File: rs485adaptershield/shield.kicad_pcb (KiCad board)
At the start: 2 copper layers, 68.6 x 53.3 mm, 8 parts, among them U2 Analog_1, U3 Analog_2, U6 Digital_1, U7 Digital_2

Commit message: schematic mostly finished w/o footprints
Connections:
- U2 pad 4: unconnected-(U2-Pad4) -> +3.3V
- U2 pad 5: unconnected-(U2-Pad5) -> +5V
- U2 pad 6: unconnected-(U2-Pad6) -> GND
- U2 pad 7: unconnected-(U2-Pad7) -> GND
- U2 pad 8: unconnected-(U2-Pad8) -> VBATT
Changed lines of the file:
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@@
 			)
 		)
-		(sheetfile "ArduinoUnoR4Shield.kicad_sch")
+		(property ki_fp_filters "MountingHole*")
+		(sheetname "/")
+		(sheetfile "shield.kicad_sch")
+		(units
+			(unit
+				(name "A")
+				(pins)
+			)
+		)
 		(attr smd)
 		(duplicate_pad_numbers_are_jumpers no)
@@
 			)
 		)
-		(sheetfile "ArduinoUnoR4Shield.kicad_sch")
+		(sheetname "/")
+		(sheetfile "shield.kicad_sch")
+		(units
+			(unit
+				(name "A")
+				(pins "11" "12" "13" "14" "15" "16" "17" "18")
+			)
+		)
 		(attr through_hole)
 		(duplicate_pad_numbers_are_jumpers no)
@@
 			(layers "*.Cu" "*.Mask")
 			(remove_unused_layers no)
-			(net "unconnected-(U7-Pad11)")
-			(pinfunction "D7")
+			(net "unconnected-(U7-D7-Pad11)")
+			(pinfunction "D7_11")
 			(pintype "bidirectional")
 		)
@@
 			(layers "*.Cu" "*.Mask")
 			(remove_unused_layers no)
-			(net "unconnected-(U7-Pad12)")
-			(pinfunction "~D6")
+			(net "unconnected-(U7-~D6-Pad12)")
+			(pinfunction "~D6_12")
 			(pintype "bidirectional")
 		)
@@
 			(layers "*.Cu" "*.Mask")
 			(remove_unused_layers no)
-			(net "unconnected-(U7-Pad13)")
-			(pinfunction "~D5")
+			(net "unconnected-(U7-~D5-Pad13)")
+			(pinfunction "~D5_13")
 			(pintype "bidirectional")
 		)
@@
 			(layers "*.Cu" "*.Mask")
 			(remove_unused_layers no)
-			(net "unconnected-(U7-Pad14)")
-			(pinfunction "D4")
+			(net "unconnected-(U7-D4-Pad14)")
+			(pinfunction "D4_14")
 			(pintype "bidirectional")
 		)
@@
 			(layers "*.Cu" "*.Mask")
 			(remove_unused_layers no)
-			(net "unconnected-(U7-Pad15)")
-			(pinfunction "~D3")
+			(net "unconnected-(U7-~D3-Pad15)")
+			(pinfunction "~D3_15")
 			(pintype "bidirectional")
 		)
@@
 			(layers "*.Cu" "*.Mask")
 			(remove_unused_layers no)
-			(net "unconnected-(U7-Pad16)")
-			(pinfunction "D2")
+			(net "unconnected-(U7-D2-Pad16)")
+			(pinfunction "D2_16")
 			(pintype "bidirectional")
 		)
@@
 			(layers "*.Cu" "*.Mask")
 			(remove_unused_layers no)
-			(net "unconnected-(U7-Pad17)")
-			(pinfunction "D1/TX0")
+			(net "unconnected-(U7-D1{slash}TX0-Pad17)")
+			(pinfunction "D1/TX0_17")
 			(pintype "bidirectional")
 		)
@@
 			(layers "*.Cu" "*.Mask")
 			(remove_unused_layers no)
-			(net "unconnected-(U7-Pad18)")
-			(pinfunction "D0/RX0")
+			(net "unconnected-(U7-D0{slash}RX0-Pad18)")
+			(pinfunction "D0/RX0_18")
 			(pintype "bidirectional")
 		)
@@
 			)
 		)
-		(sheetfile "ArduinoUnoR4Shield.kicad_sch")
+		(sheetname "/")
+		(sheetfile "shield.kicad_sch")
+		(units
+			(unit
+				(name "A")
+				(pins "1" "2" "3" "4" "5" "6" "7" "8" "9" "10")
+			)
+		)
 		(attr through_hole)
 		(duplicate_pad_numbers_are_jumpers no)
@@
 			(layers "*.Cu" "*.Mask")
 			(remove_unused_layers no)
-			(net "unconnected-(U6-Pad1)")
-			(pinfunction "SCL")
+			(net "unconnected-(U6-SCL-Pad1)")
+			(pinfunction "SCL_1")
 			(pintype "bidirectional")
 		)
@@
 			(layers "*.Cu" "*.Mask")
 			(remove_unused_layers no)
-			(net "unconnected-(U6-Pad2)")
-			(pinfunction "SDA")
+			(net "unconnected-(U6-SDA-Pad2)")
+			(pinfunction "SDA_2")
 			(pintype "bidirectional")
 		)
@@
 			(layers "*.Cu" "*.Mask")
 			(remove_unused_layers no)
-			(net "unconnected-(U6-Pad3)")
-			(pinfunction "AREF")
+			(net "unconnected-(U6-AREF-Pad3)")
+			(pinfunction "AREF_3")
 			(pintype "output")
 		)
@@
 			(layers "*.Cu" "*.Mask")
 			(remove_unused_layers no)
-			(net "unconnected-(U6-Pad4)")
-			(pinfunction "GND")
+			(net "unconnected-(U6-GND-Pad4)")
+			(pinfunction "GND_4")
 			(pintype "power_out")
 		)
@@
 			(layers "*.Cu" "*.Mask")
 			(remove_unused_layers no)
-			(net "unconnected-(U6-Pad5)")
-			(pinfunction "D13/SCK/CANRX0")
+			(net "unconnected-(U6-D13{slash}SCK{slash}CANRX0-Pad5)")
+			(pinfunction "D13/SCK/CANRX0_5")
 			(pintype "bidirectional")
 		)
@@
 			(layers "*.Cu" "*.Mask")
 			(remove_unused_layers no)
-			(net "unconnected-(U6-Pad6)")
-			(pinfunction "D12/CIPO")
+			(net "unconnected-(U6-D12{slash}CIPO-Pad6)")
+			(pinfunction "D12/CIPO_6")
 			(pintype "bidirectional")
 		)
@@
 			(layers "*.Cu" "*.Mask")
 			(remove_unused_layers no)
-			(net "unconnected-(U6-Pad7)")
-			(pinfunction "~D11/COPI")
+			(net "unconnected-(U6-~D11{slash}COPI-Pad7)")
+			(pinfunction "~D11/COPI_7")
 			(pintype "bidirectional")
 		)
@@
 			(layers "*.Cu" "*.Mask")
 			(remove_unused_layers no)
-			(net "unconnected-(U6-Pad8)")
-			(pinfunction "~D10/CS/CANTX0")
+			(net "unconnected-(U6-~D10{slash}CS{slash}CANTX0-Pad8)")
+			(pinfunction "~D10/CS/CANTX0_8")
 			(pintype "bidirectional")
 		)
@@
 			(layers "*.Cu" "*.Mask")
 			(remove_unused_layers no)
-			(net "unconnected-(U6-Pad9)")
-			(pinfunction "~D9")
+			(net "unconnected-(U6-~D9-Pad9)")
+			(pinfunction "~D9_9")
 			(pintype "bidirectional")
 		)
@@
 			(layers "*.Cu" "*.Mask")
 			(remove_unused_layers no)
-			(net "unconnected-(U6-Pad10)")
-			(pinfunction "D8")
+			(net "unconnected-(U6-D8-Pad10)")
+			(pinfunction "D8_10")
 			(pintype "bidirectional")
 		)
@@
 			)
 		)
-		(sheetfile "ArduinoUnoR4Shield.kicad_sch")
+		(property ki_fp_filters "MountingHole*")
+		(sheetname "/")
+		(sheetfile "shield.kicad_sch")
+		(units
+			(unit
+				(name "A")
+				(pins)
+			)
+		)
 		(attr smd)
 		(duplicate_pad_numbers_are_jumpers no)
@@
 			)
 		)
-		(sheetfile "ArduinoUnoR4Shield.kicad_sch")
+		(sheetname "/")
+		(sheetfile "shield.kicad_sch")
+		(units
+			(unit
+				(name "A")
+				(pins "9" "10" "11" "12" "13" "14")
+			)
+		)
 		(attr through_hole)
 		(duplicate_pad_numbers_are_jumpers no)
@@
 			(layers "*.Cu" "*.Mask")
 			(remove_unused_layers no)
-			(net "unconnected-(U3-Pad9)")
-			(pinfunction "A0")
+			(net "unconnected-(U3-A0-Pad9)")
+			(pinfunction "A0_9")
 			(pintype "bidirectional")
 		)
@@
 			(layers "*.Cu" "*.Mask")
 			(remove_unused_layers no)
-			(net "unconnected-(U3-Pad10)")
-			(pinfunction "A1")
+			(net "unconnected-(U3-A1-Pad10)")
+			(pinfunction "A1_10")
 			(pintype "bidirectional")
 		)
@@
 			(layers "*.Cu" "*.Mask")
 			(remove_unused_layers no)
-			(net "unconnected-(U3-Pad11)")
-			(pinfunction "A2")
+			(net "unconnected-(U3-A2-Pad11)")
+			(pinfunction "A2_11")
 			(pintype "bidirectional")
 		)
@@
 			(layers "*.Cu" "*.Mask")
 			(remove_unused_layers no)
-			(net "unconnected-(U3-Pad12)")
-			(pinfunction "A3")
+			(net "unconnected-(U3-A3-Pad12)")
+			(pinfunction "A3_12")
 			(pintype "bidirectional")
 		)
@@
 			(layers "*.Cu" "*.Mask")
 			(remove_unused_layers no)
-			(net "unconnected-(U3-Pad13)")
-			(pinfunction "A4")
+			(net "unconnected-(U3-A4-Pad13)")
+			(pinfunction "A4_13")
 			(pintype "bidirectional")
 		)
@@
 			(layers "*.Cu" "*.Mask")
 			(remove_unused_layers no)
-			(net "unconnected-(U3-Pad14)")
-			(pinfunction "A5")
+			(net "unconnected-(U3-A5-Pad14)")
+			(pinfunction "A5_14")
 			(pintype "bidirectional")
 		)
@@
 			)
 		)
-		(sheetfile "ArduinoUnoR4Shield.kicad_sch")
+		(sheetname "/")
+		(sheetfile "shield.kicad_sch")
+		(units
+			(unit
+				(name "A")
+				(pins "1" "2" "3" "4" "5" "6" "7" "8")
+			)
+		)
 		(attr through_hole)
 		(duplicate_pad_numbers_are_jumpers no)
@@
 			(layers "*.Cu" "*.Mask")
 			(remove_unused_layers no)
-			(net "unconnected-(U2-Pad1)")
-			(pinfunction "BOOT")
+			(net "unconnected-(U2-BOOT-Pad1)")
+			(pinfunction "BOOT_1")
 			(pintype "input")
 		)
@@
 			(layers "*.Cu" "*.Mask")
 			(remove_unused_layers no)
-			(net "unconnected-(U2-Pad2)")
-			(pinfunction "IOREF")
+			(net "unconnected-(U2-IOREF-Pad2)")
+			(pinfunction "IOREF_2")
 			(pintype "power_out")
 		)
@@
 			(layers "*.Cu" "*.Mask")
 			(remove_unused_layers no)
-			(net "unconnected-(U2-Pad3)")
-			(pinfunction "Reset")
+			(net "unconnected-(U2-Reset-Pad3)")
+			(pinfunction "Reset_3")
 			(pintype "input")
 		)
@@
 			(layers "*.Cu" "*.Mask")
 			(remove_unused_layers no)
-			(net "unconnected-(U2-Pad4)")
-			(pinfunction "+3V3")
+			(net "+3.3V")
+			(pinfunction "+3V3_4")
 			(pintype "power_out")
 		)
@@
 			(layers "*.Cu" "*.Mask")
 			(remove_unused_layers no)
-			(net "unconnected-(U2-Pad5)")
-			(pinfunction "+5V")
+			(net "+5V")
+			(pinfunction "+5V_5")
 			(pintype "power_out")
 		)
@@
 			(layers "*.Cu" "*.Mask")
 			(remove_unused_layers no)
-			(net "unconnected-(U2-Pad6)")
-			(pinfunction "GND")
+			(net "GND")
+			(pinfunction "GND_6")
 			(pintype "power_out")
 		)
@@
 			(layers "*.Cu" "*.Mask")
 			(remove_unused_layers no)
-			(net "unconnected-(U2-Pad7)")
-			(pinfunction "GND")
+			(net "GND")
+			(pinfunction "GND_7")
 			(pintype "power_out")
 		)
@@
 			(layers "*.Cu" "*.Mask")
 			(remove_unused_layers no)
-			(net "unconnected-(U2-Pad8)")
-			(pinfunction "VIN")
+			(net "VBATT")
+			(pinfunction "VIN_8")
 			(pintype "power_out")
 		)
@@
 			)
 		)
-		(sheetfile "ArduinoUnoR4Shield.kicad_sch")
+		(property ki_fp_filters "MountingHole*")
+		(sheetname "/")
+		(sheetfile "shield.kicad_sch")
+		(units
+			(unit
+				(name "A")
+				(pins)
+			)
+		)
 		(attr smd)
 		(duplicate_pad_numbers_are_jumpers no)
@@
 			)
 		)
-		(sheetfile "ArduinoUnoR4Shield.kicad_sch")
+		(property ki_fp_filters "MountingHole*")
+		(sheetname "/")
+		(sheetfile "shield.kicad_sch")
+		(units
+			(unit
+				(name "A")
+				(pins)
+			)
+		)
 		(attr smd)
 		(duplicate_pad_numbers_are_jumpers no)

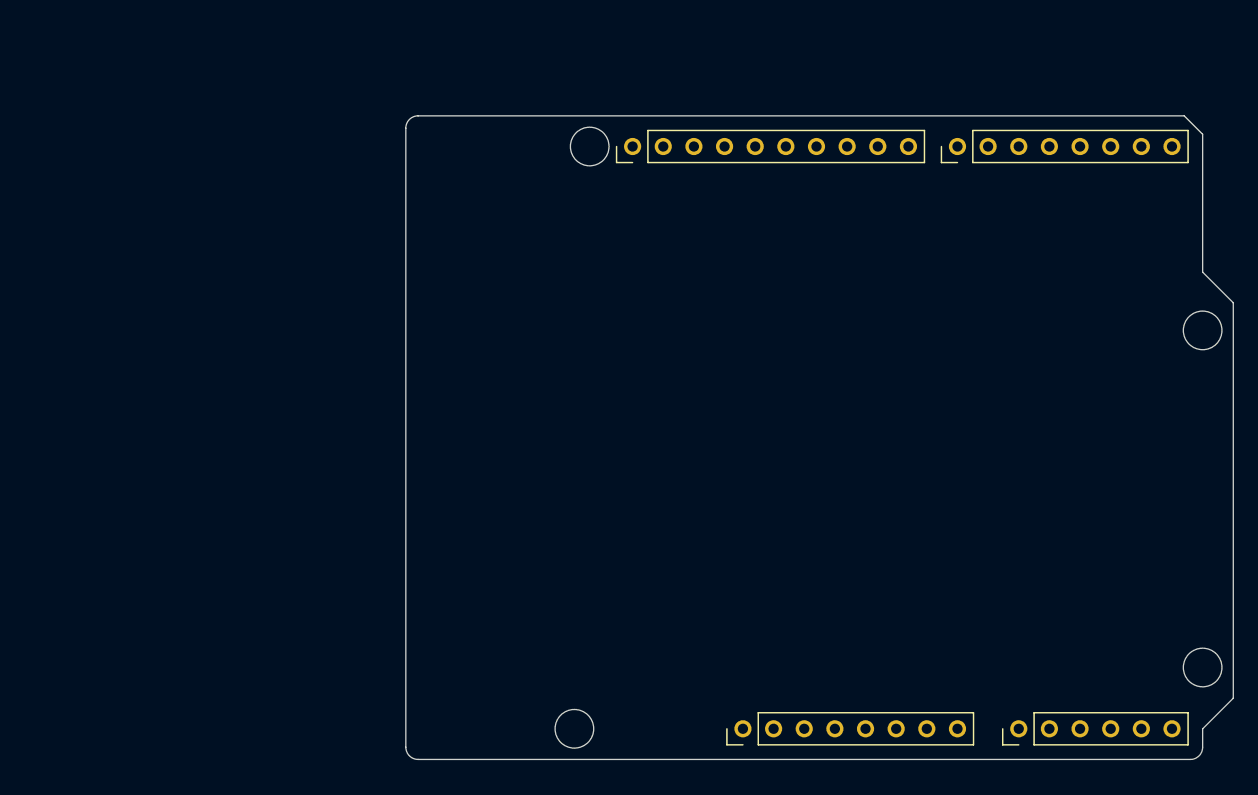
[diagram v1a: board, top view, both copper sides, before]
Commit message: usb stackup problems
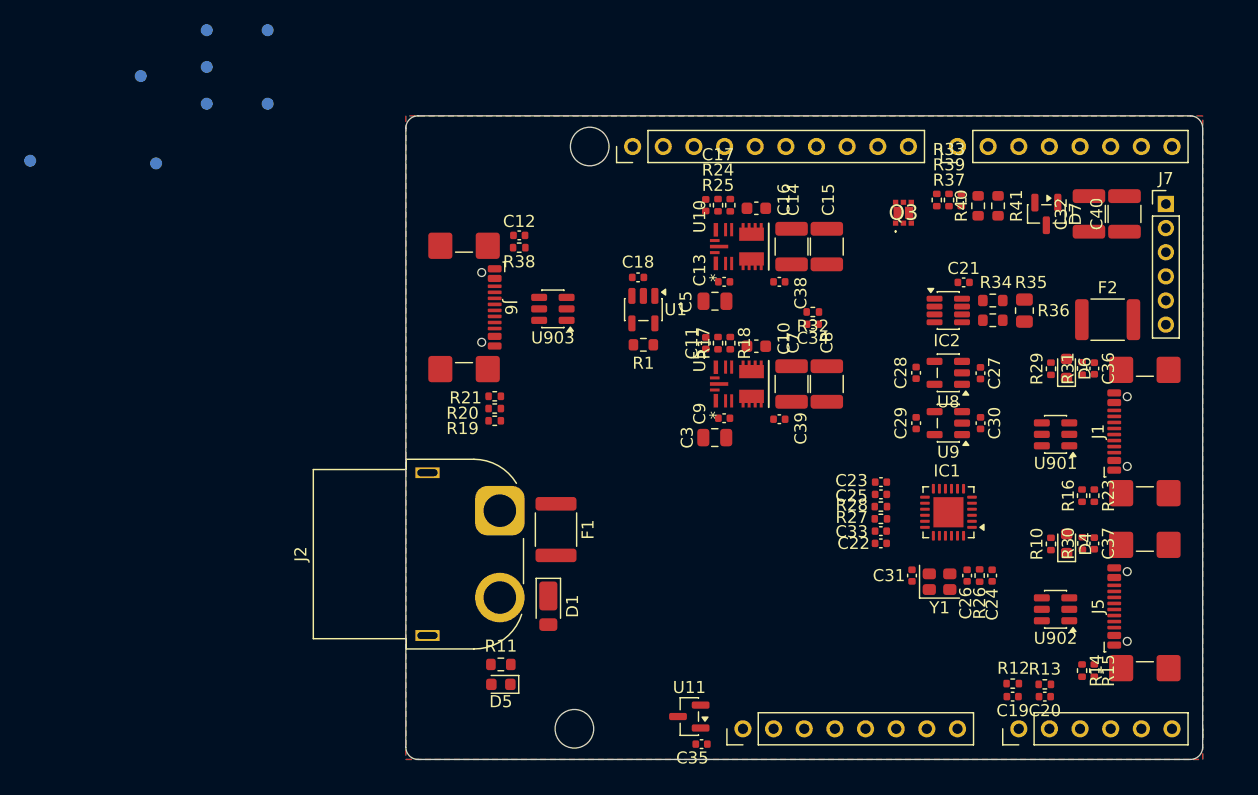
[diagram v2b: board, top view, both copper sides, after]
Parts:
- removed H1: MountingHole1, ArduinoMountingHoles:Arduino_MountingHole
- removed H3: MountingHole3, ArduinoMountingHoles:Arduino_MountingHole
- added C10: 1u, Capacitor_SMD:C_0603_1608Metric, F.Cu at (135.7, 85.1)
- added C11: 10p, Capacitor_SMD:C_0402_1005Metric, F.Cu at (131.5, 84.9)
- added C12: 100n, Capacitor_SMD:C_0402_1005Metric, F.Cu at (116.1, 75.9)
- added C13: 100n, Capacitor_SMD:C_0402_1005Metric, F.Cu at (133.1, 79.8)
- added C14: 22u, Capacitor_SMD:C_1210_3225Metric, F.Cu at (138.6, 76.9)
- added C15: 22u, Capacitor_SMD:C_1210_3225Metric, F.Cu at (141.6, 76.9)
- added C16: 1u, Capacitor_SMD:C_0603_1608Metric, F.Cu at (135.7, 73.7)
- added C17: 10p, Capacitor_SMD:C_0402_1005Metric, F.Cu at (131.5, 73.4)
- added C18: 100n, Capacitor_SMD:C_0402_1005Metric, F.Cu at (125.9, 79.4)
- added C19: 100n, Capacitor_SMD:C_0402_1005Metric, F.Cu at (157.0, 114.2)
- added C20: 100n, Capacitor_SMD:C_0402_1005Metric, F.Cu at (159.6, 114.2)
- added C21: 100n, Capacitor_SMD:C_0402_1005Metric, F.Cu at (152.9, 79.8)
- added C22: 100n, Capacitor_SMD:C_0402_1005Metric, F.Cu at (146.1, 101.5)
- added C23: 100n, Capacitor_SMD:C_0402_1005Metric, F.Cu at (146.1, 96.4)
- added C24: 1u, Capacitor_SMD:C_0402_1005Metric, F.Cu at (155.3, 104.1)
- added C25: 1u, Capacitor_SMD:C_0402_1005Metric, F.Cu at (146.1, 97.4)
- added C26: 100n, Capacitor_SMD:C_0402_1005Metric, F.Cu at (153.2, 104.1)
- added C27: 100n, Capacitor_SMD:C_0402_1005Metric, F.Cu at (154.3, 87.4)
- added C28: 100n, Capacitor_SMD:C_0402_1005Metric, F.Cu at (149.0, 87.3)
- added C29: 100n, Capacitor_SMD:C_0402_1005Metric, F.Cu at (149.0, 91.5)
- added C3: 4.7u, Capacitor_SMD:C_0805_2012Metric, F.Cu at (132.3, 92.7)
- added C30: 100n, Capacitor_SMD:C_0402_1005Metric, F.Cu at (154.3, 91.5)
- added C31: 100n, Capacitor_SMD:C_0402_1005Metric, F.Cu at (148.6, 104.1)
- added C32: 22u, Capacitor_SMD:C_1210_3225Metric, F.Cu at (163.3, 74.2)
- added C33: 100n, Capacitor_SMD:C_0402_1005Metric, F.Cu at (146.1, 100.5)
- added C34: 100n, Capacitor_SMD:C_0402_1005Metric, F.Cu at (140.4, 83.3)
- added C35: 100n, Capacitor_SMD:C_0402_1005Metric, F.Cu at (131.2, 118.1)
- added C36: 100n, Capacitor_SMD:C_0402_1005Metric, F.Cu at (163.7, 87.0)
- added C37: 100n, Capacitor_SMD:C_0402_1005Metric, F.Cu at (163.7, 101.5)
- added C38: 100n, Capacitor_SMD:C_0402_1005Metric, F.Cu at (137.6, 79.8)
- added C39: 100n, Capacitor_SMD:C_0402_1005Metric, F.Cu at (137.6, 91.2)
- added C40: 22u, Capacitor_SMD:C_1210_3225Metric, F.Cu at (166.2, 74.2)
- added C5: 4.7u, Capacitor_SMD:C_0805_2012Metric, F.Cu at (132.3, 81.4)
- added C7: 22u, Capacitor_SMD:C_1210_3225Metric, F.Cu at (138.6, 88.3)
- added C8: 22u, Capacitor_SMD:C_1210_3225Metric, F.Cu at (141.6, 88.3)
- added C9: 100n, Capacitor_SMD:C_0402_1005Metric, F.Cu at (133.1, 91.1)
- added D1: SBR3U60P1-7, Diode_SMD:D_PowerDI-123, F.Cu at (118.5, 106.7)
- added D4: LED, LED_SMD:LED_0603_1608Metric, F.Cu at (161.4, 101.5)
- added D5: LED, LED_SMD:LED_0603_1608Metric, F.Cu at (114.6, 113.2)
- added D6: LED, LED_SMD:LED_0603_1608Metric, F.Cu at (161.4, 87.0)
- added D7: SM712_SOT23, Package_TO_SOT_SMD:SOT-23, F.Cu at (159.8, 74.2)
- added F1: 13A, Fuse:Fuse_1812_4532Metric, F.Cu at (119.1, 100.3)
- added F2: 13A, Fuse:Fuse_1812_4532Metric, F.Cu at (164.8, 82.9)
- added IC1: USB2422-I_MJ, Package_DFN_QFN:QFN-24-1EP_4x4mm_P0.5mm_EP2.5x2.5mm, F.Cu at (151.7, 98.9)
- added IC2: THVD1406DRLR, Package_TO_SOT_SMD:SOT-23-8, F.Cu at (151.6, 82.2)
- added J1: ~, Connector_USB:USB_C_Receptacle_GCT_USB4110, F.Cu at (169.1, 92.2)
- added J2: XT60, Connector_AMASS:AMASS_XT60PW-F_1x02_P7.20mm_Horizontal, F.Cu at (114.5, 98.8)
- added J5: ~, Connector_USB:USB_C_Receptacle_GCT_USB4110, F.Cu at (169.1, 106.7)
- added J6: ~, Connector_USB:USB_C_Receptacle_GCT_USB4110, F.Cu at (110.4, 81.9)
- added J7: RACK OUT 2.00mm, Connector_PinHeader_2.00mm:PinHeader_1x06_P2.00mm_Vertical, F.Cu at (169.7, 73.3)
- added Q3: UT6KE5, IMPORTED:UT6KE5TCR, F.Cu at (147.9, 74.1)
- added R1: 2m, Resistor_SMD:R_0603_1608Metric, F.Cu at (126.4, 85.0)
- added R10: 560, Resistor_SMD:R_0402_1005Metric, F.Cu at (160.1, 101.5)
- added R11: 2.1k, Resistor_SMD:R_0603_1608Metric, F.Cu at (114.6, 111.5)
- added R12: 10k, Resistor_SMD:R_0402_1005Metric, F.Cu at (157.0, 113.1)
- added R13: 10k, Resistor_SMD:R_0402_1005Metric, F.Cu at (159.6, 113.2)
- added R14: 22k, Resistor_SMD:R_0402_1005Metric, F.Cu at (162.7, 112.0)
- added R15: 22k, Resistor_SMD:R_0402_1005Metric, F.Cu at (163.7, 112.0)
- added R16: 22k, Resistor_SMD:R_0402_1005Metric, F.Cu at (162.7, 97.5)
- added R17: 47k, Resistor_SMD:R_0402_1005Metric, F.Cu at (132.6, 84.9)
- added R18: 10k, Resistor_SMD:R_0402_1005Metric, F.Cu at (133.6, 84.9)
- added R19: 5.1k, Resistor_SMD:R_0402_1005Metric, F.Cu at (114.0, 91.3)
- added R20: 5.1k, Resistor_SMD:R_0402_1005Metric, F.Cu at (114.0, 90.3)
- added R21: 5.1k, Resistor_SMD:R_0402_1005Metric, F.Cu at (114.0, 89.3)
- added R23: 22k, Resistor_SMD:R_0402_1005Metric, F.Cu at (163.7, 97.5)
- added R24: 50k, Resistor_SMD:R_0402_1005Metric, F.Cu at (132.6, 73.4)
- added R25: 12k, Resistor_SMD:R_0402_1005Metric, F.Cu at (133.6, 73.4)
- added R26: 12k, Resistor_SMD:R_0402_1005Metric, F.Cu at (154.2, 104.1)
- added R27: 100k, Resistor_SMD:R_0402_1005Metric, F.Cu at (146.1, 99.4)
- added R28: 100k, Resistor_SMD:R_0402_1005Metric, F.Cu at (146.1, 98.4)
- added R29: 560, Resistor_SMD:R_0402_1005Metric, F.Cu at (160.1, 87.0)
- added R30: 1M, Resistor_SMD:R_0402_1005Metric, F.Cu at (162.8, 101.5)
- added R31: 1M, Resistor_SMD:R_0402_1005Metric, F.Cu at (162.7, 87.0)
- added R32: 330k, Resistor_SMD:R_0402_1005Metric, F.Cu at (140.4, 82.3)
- added R33: 10k, Resistor_SMD:R_0402_1005Metric, F.Cu at (152.7, 73.0)
- added R34: 10, Resistor_SMD:R_0603_1608Metric, F.Cu at (155.3, 83.0)
- added R35: 10, Resistor_SMD:R_0603_1608Metric, F.Cu at (155.3, 81.3)
- added R36: 120, Resistor_SMD:R_0805_2012Metric, F.Cu at (157.9, 82.2)
- added R37: 10k, Resistor_SMD:R_0402_1005Metric, F.Cu at (150.7, 73.0)
- added R38: 1M, Resistor_SMD:R_0402_1005Metric, F.Cu at (116.1, 77.0)
- added R39: 10k, Resistor_SMD:R_0402_1005Metric, F.Cu at (151.7, 73.0)
- added R40: 1, Resistor_SMD:R_0603_1608Metric, F.Cu at (154.1, 73.5)
- added R41: 1, Resistor_SMD:R_0603_1608Metric, F.Cu at (155.8, 73.5)
- added TP1: FB_REG_2, TestPoint:TestPoint_Pad_D1.0mm, B.Cu at (95.2, 58.9)
- added TP2: FB_REG_1, TestPoint:TestPoint_Pad_D1.0mm, B.Cu at (75.5, 69.8)
- added TP4: USB_PSU_EN, TestPoint:TestPoint_Pad_D1.0mm, B.Cu at (95.2, 65.0)
- added TP5: USB_HUB_RST, TestPoint:TestPoint_Pad_D1.0mm, B.Cu at (90.2, 58.9)
- added TP6: USB1_VBUS, TestPoint:TestPoint_Pad_D1.0mm, B.Cu at (90.2, 62.0)
- added TP7: USB2_VBUS, TestPoint:TestPoint_Pad_D1.0mm, B.Cu at (90.2, 65.0)
- added TP8: USB1_VREG, TestPoint:TestPoint_Pad_D1.0mm, B.Cu at (86.0, 70.0)
- added TP9: USB2_VREG, TestPoint:TestPoint_Pad_D1.0mm, B.Cu at (84.7, 62.7)
- added U1: INA293B3, Package_TO_SOT_SMD:SOT-23-5, F.Cu at (126.4, 82.1)
- added U10: TPSM33606S5QRDNRQ1, IMPORTED:RDN0011A_TEX, F.Cu at (134.3, 76.9)
- added U11: MCP9700Ax-ETT, Package_TO_SOT_SMD:SOT-23, F.Cu at (130.2, 115.8)
- added U5: TPSM33606S5QRDNRQ1, IMPORTED:RDN0011A_TEX, F.Cu at (134.3, 88.3)
- added U8: AP2171W, Package_TO_SOT_SMD:SOT-23-5, F.Cu at (151.6, 87.3)
- added U9: AP2171W, Package_TO_SOT_SMD:SOT-23-5, F.Cu at (151.6, 91.5)
- added U901: USBLC6-2SC6, Package_TO_SOT_SMD:SOT-23-6, F.Cu at (160.5, 92.4)
- added U902: USBLC6-2SC6, Package_TO_SOT_SMD:SOT-23-6, F.Cu at (160.5, 106.9)
- added U903: USBLC6-2SC6, Package_TO_SOT_SMD:SOT-23-6, F.Cu at (118.9, 82.0)
- added Y1: SG-210STF, Oscillator:Oscillator_SMD_SeikoEpson_SG210-4Pin_2.5x2.0mm, F.Cu at (150.9, 104.6)
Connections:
- U3 pad 10: unconnected-(U3-A1-Pad10) -> /T_SENSE
- U3 pad 9: unconnected-(U3-A0-Pad9) -> /I_SENSE
- U7 pad 11: unconnected-(U7-D7-Pad11) -> /USB_PSU_EN
- U7 pad 12: unconnected-(U7-~D6-Pad12) -> /¬USB_HUB_RST
- U7 pad 16: unconnected-(U7-D2-Pad16) -> /RS485 TxRx/¬RE
- U7 pad 17: unconnected-(U7-D1/TX0-Pad17) -> /RS485 TxRx/D
- U7 pad 18: unconnected-(U7-D0/RX0-Pad18) -> /RS485 TxRx/R
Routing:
- added copper zone on B.Cu, net GND
- added copper zone on F.Cu, net GND
- added copper zone on In1.Cu, net GND
- added copper zone on In2.Cu, net GND
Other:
- board size 68.6 x 53.3 mm -> 66 x 53.3 mm
- copper layers 2 -> 4

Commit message: netclass bullshit
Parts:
- removed U903: USBLC6-2SC6, Package_TO_SOT_SMD:SOT-23-6
- moved U11 30.3 mm to (160.0, 110.9), turned to 0 degrees
- moved C35 27.3 mm to (157.5, 110.9), turned to 90 degrees
- moved C18 23.3 mm to (124.7, 102.7), turned to 0 degrees
- moved U1 23.1 mm to (123.7, 105.0), turned to 180 degrees
- moved R1 20.8 mm to (120.8, 105.0), turned to -90 degrees
- moved U901 1.54 mm to (162.1, 92.2)
- moved U902 1.54 mm to (162.1, 106.7)
- moved D1 0.64 mm to (118.5, 106.0), turned to 90 degrees
- moved R36 0.13 mm to (157.9, 82.1)
- moved C21 0.13 mm to (152.9, 79.7)
- moved IC2 0.13 mm to (151.6, 82.0)
- moved R34 0.13 mm to (155.3, 82.9)
- moved R35 0.13 mm to (155.3, 81.2)
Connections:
- net Net-(J1-D+-PadA6) renamed /DCONN_1+
- net Net-(J1-D--PadA7) renamed /DCONN_1-
- net Net-(J5-D+-PadA6) renamed /DCONN_2+
- net Net-(J5-D--PadA7) renamed /DCONN_2-
- C33 pad 2: /USB/¬RESET -> /¬USB_HUB_RST
- D1 pad 1: /Current and Temp Sense/R_SENSE+ -> VBATT
- IC1 pad 15: /USB/¬RESET -> /¬USB_HUB_RST
- IC1 pad 19: /USB/USB_HOST- -> /DI-
- IC1 pad 20: /USB/USB_HOST+ -> /DI+
- J6 pad A6: /DIN+ -> /DI+
- J6 pad A7: /DIN- -> /DI-
- J6 pad B6: /DIN+ -> /DI+
- J6 pad B7: /DIN- -> /DI-
- R27 pad 2: /USB/¬RESET -> /¬USB_HUB_RST
- TP5 pad 1: /USB/¬RESET -> /¬USB_HUB_RST
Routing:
- net /DI+: track 0.00 -> 56.7 mm
- net /DI-: track 0.00 -> 56.5 mm
- net /DB-: track 0.00 -> 13.2 mm
- net /DB+: track 0.00 -> 13.2 mm
- net /DA+: track 0.00 -> 12.4 mm
- net /DA-: track 0.00 -> 12.4 mm
- net +3.3V: track 0.00 -> 8.46 mm
- net /DCONN_1+: track 0.00 -> 4.77 mm
- net /DCONN_2+: track 0.00 -> 4.66 mm
- net /¬USB_HUB_RST: track 0.00 -> 4.50 mm
- net /DCONN_1-: track 0.00 -> 4.08 mm
- net /DCONN_2-: track 0.00 -> 4.02 mm
- net /I_SENSE: track 0.00 -> 3.75 mm
- net /T_SENSE: track 0.00 -> 3.74 mm
- net /USB/RBIAS: track 0.00 -> 3.34 mm
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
